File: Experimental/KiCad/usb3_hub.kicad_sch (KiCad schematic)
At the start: 75 parts, among them IC10 TPS62933ODRLR, IC11 FUSB303BTMX, IC12 TPS2068E, IC9 USB5816C-I/KD, X6 USB4056-03-A, Y2 VXM7-9032-25M0000000

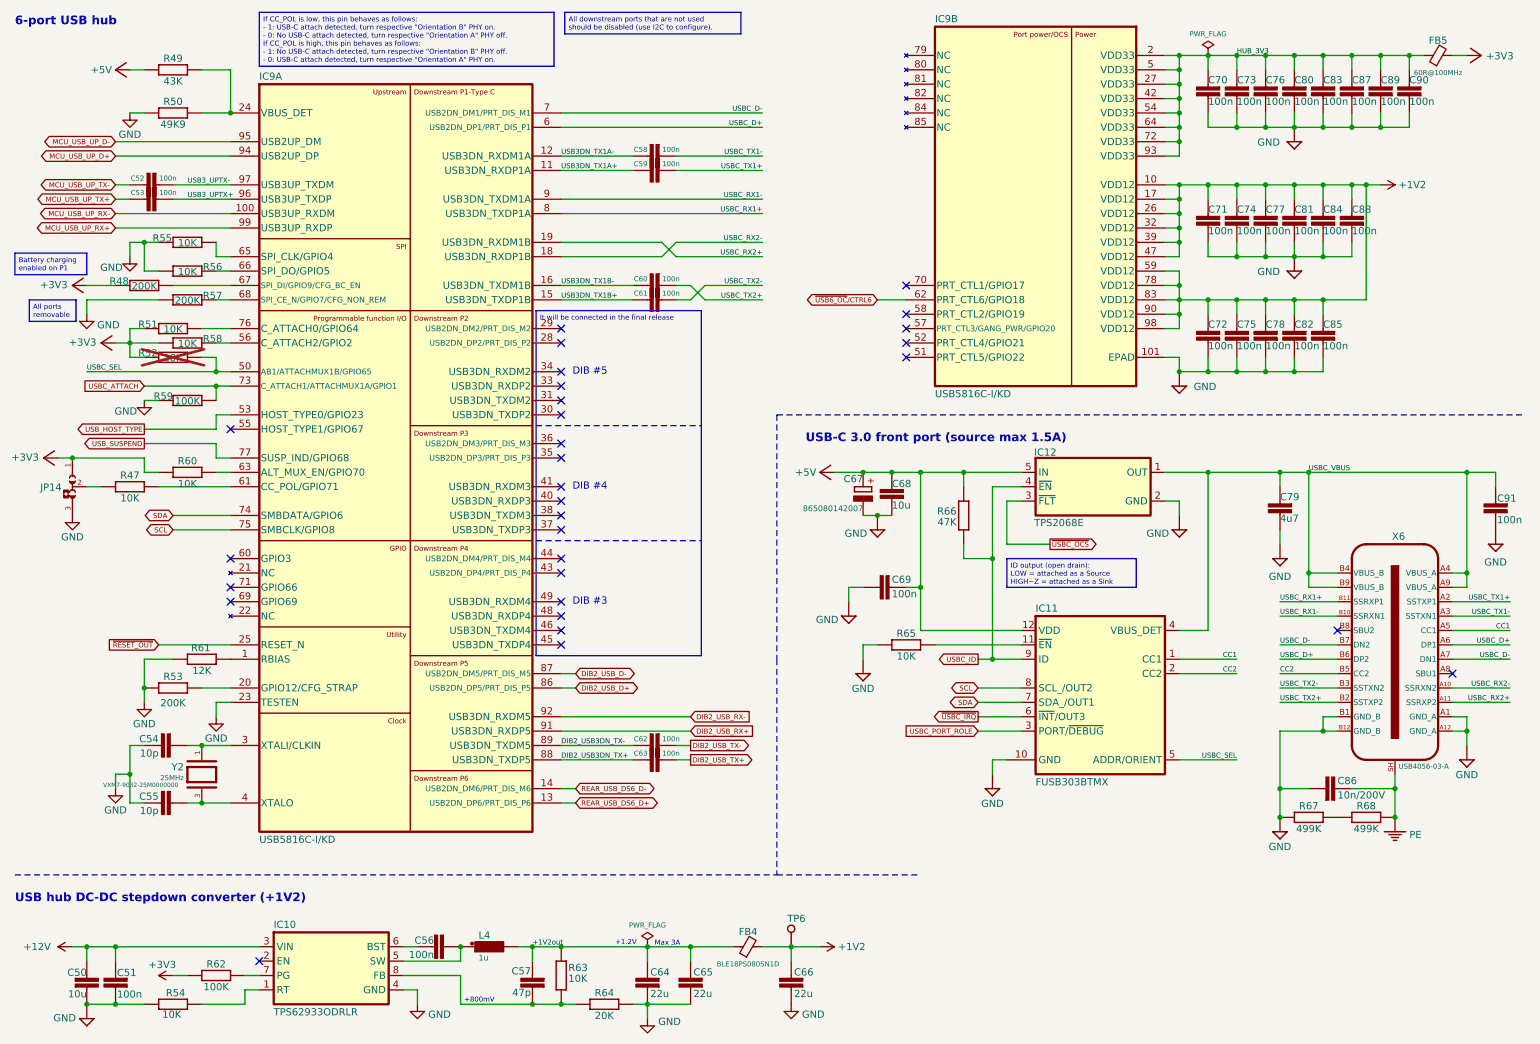
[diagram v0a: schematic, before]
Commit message: Replace 3V3 jumper for H7 CM5 with PMOS sw
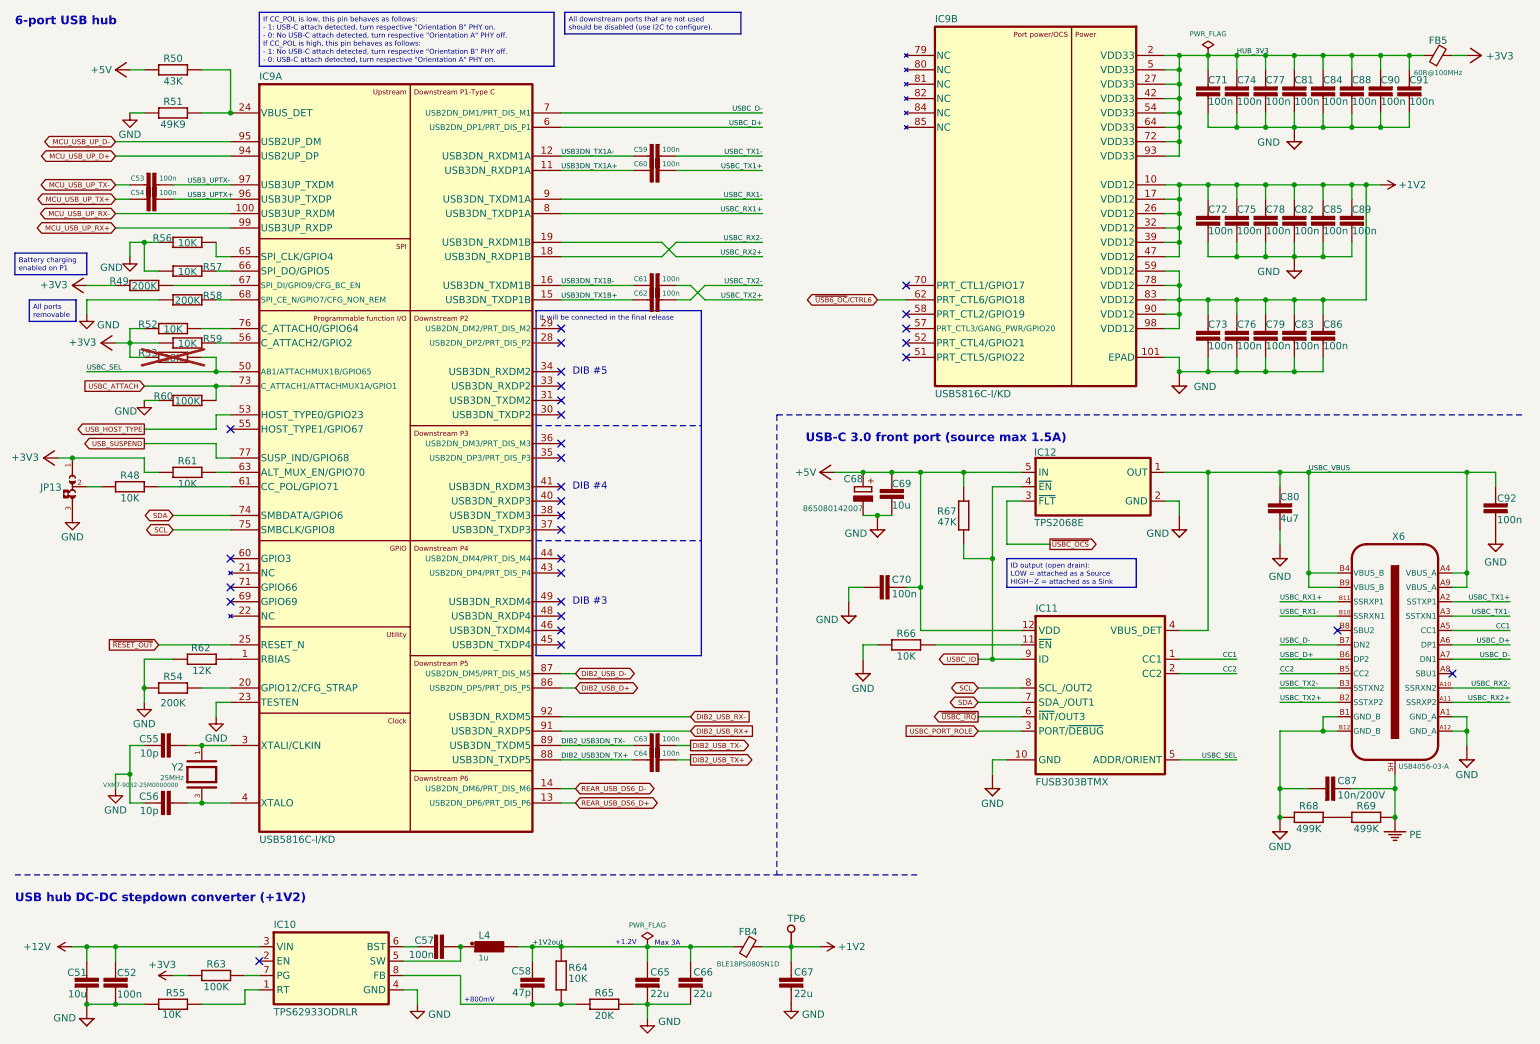
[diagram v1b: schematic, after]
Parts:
- renumbered C50 to C51, C51 to C52, C52 to C53, C53 to C54, C54 to C55, C55 to C56, C56 to C57, C57 to C58, C58 to C59, C59 to C60, C60 to C61, C61 to C62, C62 to C63, C63 to C64, C64 to C65, C65 to C66, C66 to C67, C67 to C68, C68 to C69, C69 to C70, C70 to C71, C71 to C72, C72 to C73, C73 to C74, C74 to C75, C75 to C76, C76 to C77, C77 to C78, C78 to C79, C79 to C80, C80 to C81, C81 to C82, C82 to C83, C83 to C84, C84 to C85, C85 to C86, C86 to C87, C87 to C88, C88 to C89, C89 to C90, C90 to C91, C91 to C92, JP14 to JP13, R47 to R48, R48 to R49, R49 to R50, R50 to R51, R51 to R52, R52 to R53, R53 to R54, R54 to R55, R55 to R56, R56 to R57, R57 to R58, R58 to R59, R59 to R60, R60 to R61, R61 to R62, R62 to R63, R63 to R64, R64 to R65, R65 to R66, R66 to R67, R67 to R68, R68 to R69

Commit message: Jumpers update
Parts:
- JP13: symbol PCM_EEZ_unsorted:JP3 shorted with 0R (2-3) -> PCM_EEZ_unsorted:JP3 2mm THT (2-3)
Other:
- moved on the sheet: C67, FB4, TP6

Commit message: TFT display tactile switches footprint correction
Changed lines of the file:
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@@
 	(title_block
 		(title "${project_name}")
-		(date "2025-10-25")
+		(date "2025-11-27")
 		(rev "${project_version}")
 		(company "${project_creator}")
@@
 			)
 			(justify left top)
+		)
+	)
+	(text_box "Change to pullup for I2C\nprogramming purposes?"
+		(exclude_from_sim no)
+		(at 19.05 132.08 0)
+		(size 29.21 7.62)
+		(margins 0.9525 0.9525 0.9525 0.9525)
+		(stroke
+			(width 0)
+			(type solid)
+			(color 255 0 0 1)
+		)
+		(fill
+			(type none)
+		)
+		(effects
+			(font
+				(size 0.889 0.889)
+				(color 255 0 0 1)
+			)
+			(justify left top)
